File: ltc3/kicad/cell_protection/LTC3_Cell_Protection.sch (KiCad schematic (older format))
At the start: 80 parts, among them P301 CONN_BATT_MAIN, P303 CONN_BATT_SENSE, P305 S2BPHKS, P306 PIN_HEAD_1x2, Q301 MMBT3904, Q302 SUM110P08-11, Q303 SUM110P08-11, Q304 SUM110P08-11, Q305 SUM110P08-11, Q306 NDS9407, U301 LTC2990, U302 BQ77PL900

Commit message: LTC3: Charge Controller Layout
With boards broken up, charge controller circuitry has been re-layed out.
This commit is a rough first pass - there is no via stiching to ground
yet.
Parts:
- renumbered BT301 to BT1, BT302 to BT2, BT303 to BT3, BT304 to BT4, BT305 to BT5, BT306 to BT6, BT307 to BT7, BT308 to BT8, C313 to C1, C304 to C10, C310 to C11, C311 to C12, C312 to C13, C315 to C14, C317 to C15, C318 to C16, C319 to C17, C306 to C18, C302 to C19, C305 to C2, C301 to C20, C314 to C3, C316 to C4, C307 to C5, C303 to C6, C308 to C7, C309 to C8, C320 to C9, D301 to D1, D302 to D2, D305 to D3, D303 to D4, D306 to D5, D304 to D6, F301 to F1, P305 to P1, P306 to P2, P301 to P3, P303 to P4, P302 to P5, P304 to P6, Q302 to Q1, Q304 to Q2, Q306 to Q3, Q303 to Q4, Q305 to Q5, Q301 to Q6, R303 to R1, R324 to R10, R323 to R11, R305 to R12, R310 to R13, R312 to R14, R313 to R15, R314 to R16, R316 to R17, R317 to R18, R319 to R19, R307 to R2, R320 to R20, R321 to R21, R306 to R22, R302 to R23, R301 to R24, R308 to R3, R315 to R4, R318 to R5, R304 to R6, R309 to R7, R311 to R8, R322 to R9, U302 to U1, U301 to U2, W302 to W1, W306 to W2, W307 to W3, W304 to W4, W305 to W5, W301 to W6, W303 to W7

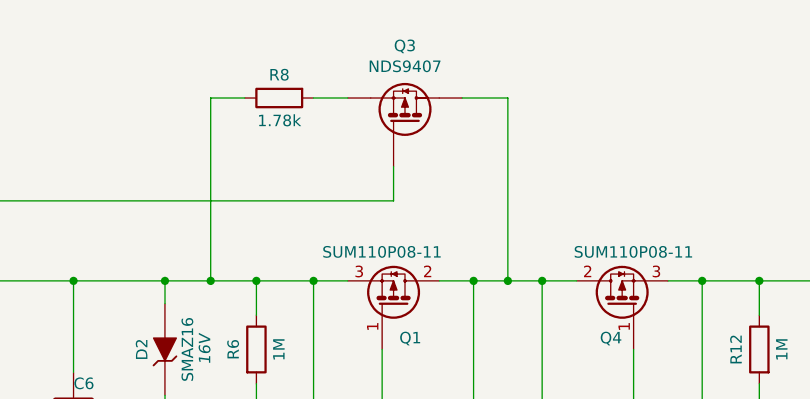
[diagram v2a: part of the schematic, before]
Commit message: LTC3: Restarted layout of Cell Protection
Began re-laying out cell protection section of LTC3.
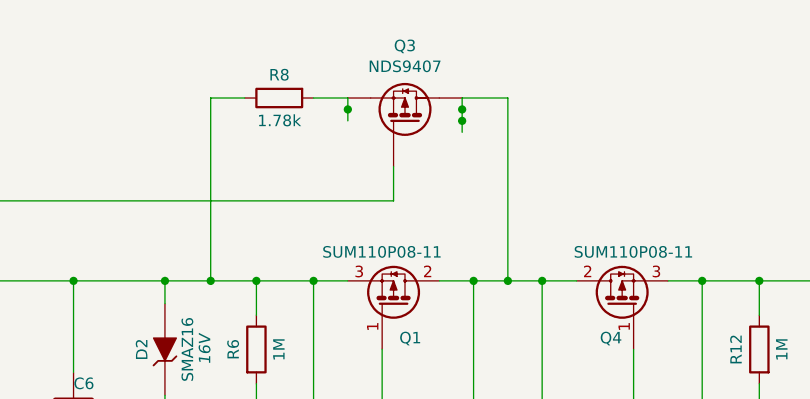
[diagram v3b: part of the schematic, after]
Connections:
- net at Q3.3 (S), R8.2: now also Q3.1 (S), Q3.2 (S)
- net at Q1.2, Q2.2, Q3.5 (D)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: now also Q3.6 (D), Q3.7 (D), Q3.8 (D)
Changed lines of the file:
@@
 Text Notes 9100 5650 0    100  ~ 20
 TODO: select connectors
+Wire Wire Line
+	4250 1100 4250 1250
+Connection ~ 4250 1150
+Connection ~ 4250 1200
+Wire Wire Line
+	3750 1100 3750 1200
+Connection ~ 3750 1150
 $EndSCHEMATC

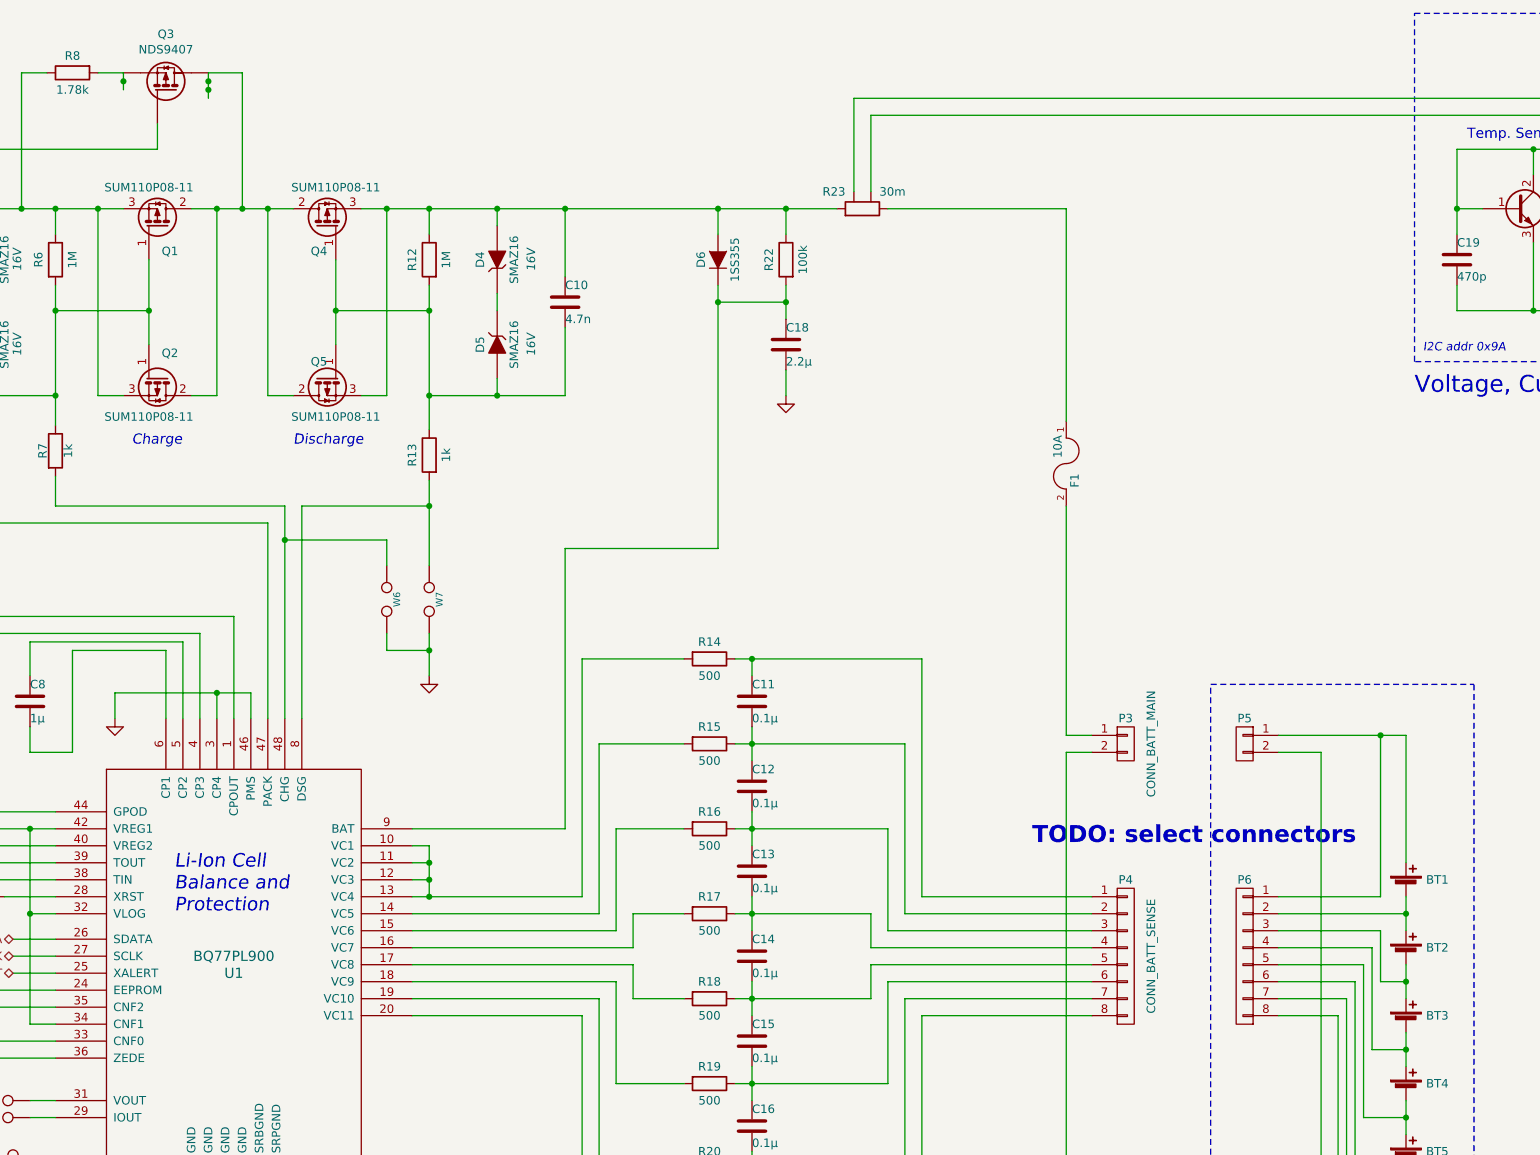
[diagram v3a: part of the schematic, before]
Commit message: LTC3: Selected battery connectors for cell protection board.
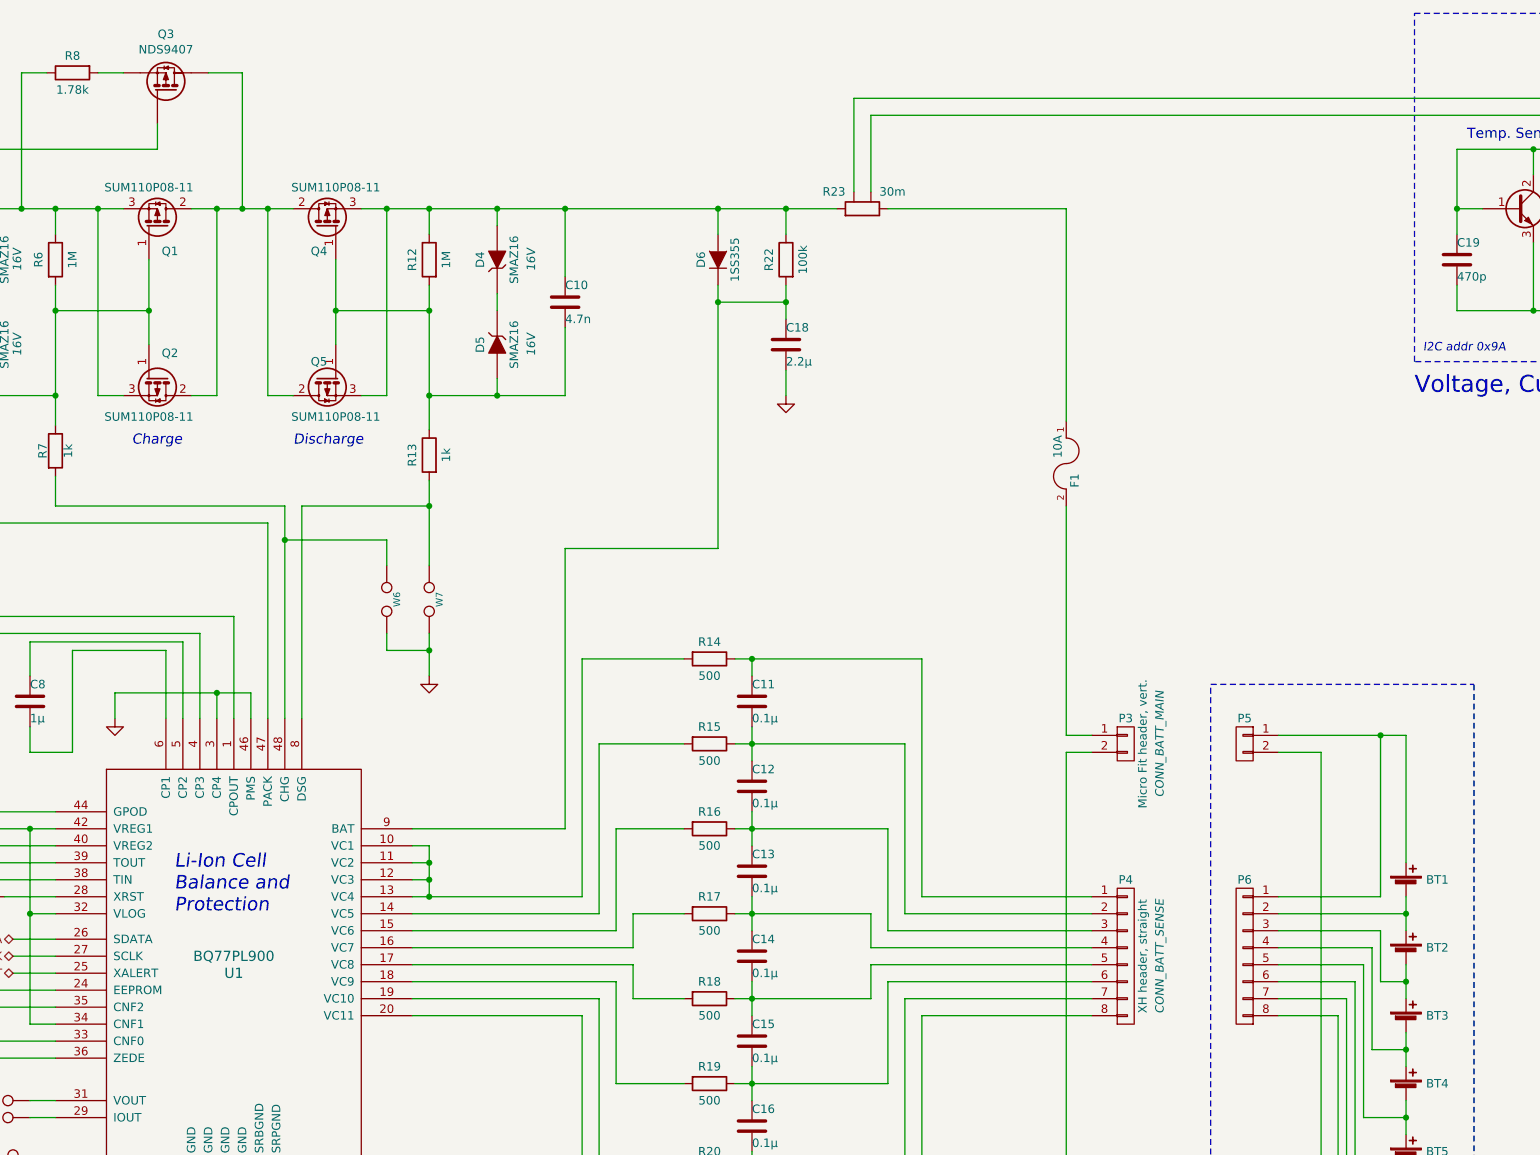
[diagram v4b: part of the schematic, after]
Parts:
- F1: Mfg_Name (none) -> Keystone; Mfg_PN (none) -> 3557-2; Note (none) -> -; Spec (none) -> -
- P3: value CONN_BATT_MAIN -> Micro Fit header, vert.; Mfg_Name (none) -> Molex; Mfg_PN (none) -> 43045-0228; Note (none) -> CONN_BATT_MAIN; Spec (none) -> -
- P4: value CONN_BATT_SENSE -> XH header, straight; footprint Connectors_Molex:Molex_Microfit3_Header_02x04_Straight_43045-0828 -> Connectors_JST:JST_XH_B08B-XH-A_08x2.50mm_Straight; Mfg_Name (none) -> JST; Mfg_PN (none) -> B8B-XH-A; Note (none) -> CONN_BATT_SENSE; Spec (none) -> -
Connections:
- net at Q3.3 (S), R8.2: no longer Q3.1 (S), Q3.2 (S)
- net at Q1.2, Q2.2, Q3.5 (D)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: no longer Q3.6 (D), Q3.7 (D), Q3.8 (D)
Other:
- note removed: "TODO: select connectors"
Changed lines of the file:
@@
 LIBS:atmel
 LIBS:audio
-LIBS:bbd
 LIBS:brooktre
 LIBS:cmos4000
@@
 P 9650 6300
 F 0 "P4" H 9650 6750 50  0000 C CNN
-F 1 "CONN_BATT_SENSE" V 9800 6300 50  0000 C CNN
-F 2 "Connectors_Molex:Molex_Microfit3_Header_02x04_Straight_43045-0828" H 9650 6300 60  0001 C CNN
-F 3 "" H 9650 6300 60  0000 C CNN
+F 1 "XH header, straight" V 9750 6300 50  0000 C CNN
+F 2 "Connectors_JST:JST_XH_B08B-XH-A_08x2.50mm_Straight" H 9650 6300 60  0001 C CNN
+F 3 "http://www.jst-mfg.com/product/pdf/eng/eXH.pdf" H 9650 6300 60  0001 C CNN
+F 4 "-" H 9650 6300 60  0001 C CNN "Spec"
+F 5 "CONN_BATT_SENSE" V 9850 6300 50  0000 C CIN "Note"
+F 6 "JST" H 9650 6300 60  0001 C CNN "Mfg_Name"
+F 7 "B8B-XH-A" H 9650 6300 60  0001 C CNN "Mfg_PN"
 	1    9650 6300
 	1    0    0    -1
@@
 P 9650 5050
 F 0 "P3" H 9650 5200 50  0000 C CNN
-F 1 "CONN_BATT_MAIN" V 9800 5050 50  0000 C CNN
+F 1 "Micro Fit header, vert." V 9750 5050 50  0000 C CNN
 F 2 "Connectors_Molex:Molex_Microfit3_Header_02x01_Straight_43045-0228" H 9650 5050 60  0001 C CNN
 F 3 "" H 9650 5050 60  0000 C CNN
+F 4 "-" H 9650 5050 60  0001 C CNN "Spec"
+F 5 "CONN_BATT_MAIN" V 9850 5050 50  0000 C CIN "Note"
+F 6 "Molex" H 9650 5050 60  0001 C CNN "Mfg_Name"
+F 7 "43045-0228" H 9650 5050 60  0001 C CNN "Mfg_PN"
 	1    9650 5050
 	1    0    0    -1
@@
 F 2 "LTC3:Fuseholder_Auto_Blade_Regular_Keystone_3557-2" H 9300 3400 60  0001 C CNN
 F 3 "" H 9300 3400 60  0000 C CNN
+F 4 "-" H 9300 3400 60  0001 C CNN "Spec"
+F 5 "-" H 9300 3400 60  0001 C CNN "Note"
+F 6 "Keystone" H 9300 3400 60  0001 C CNN "Mfg_Name"
+F 7 "3557-2" H 9300 3400 60  0001 C CNN "Mfg_PN"
 	1    9300 3400
 	0    1    1    0
@@
 Wire Wire Line
 	2100 3100 2100 3000
-Text Notes 9100 5650 0    100  ~ 20
-TODO: select connectors
-Wire Wire Line
-	4250 1100 4250 1250
-Connection ~ 4250 1150
-Connection ~ 4250 1200
-Wire Wire Line
-	3750 1100 3750 1200
-Connection ~ 3750 1150
 $EndSCHEMATC

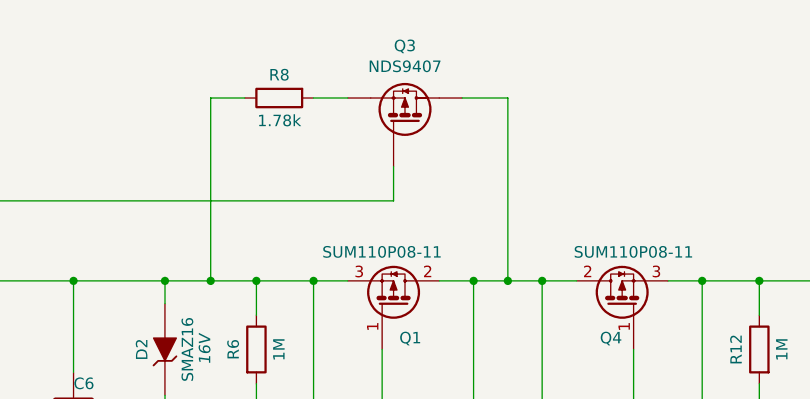
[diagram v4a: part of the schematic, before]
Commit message: LTC3: Cell Protection Layout
Made significant progress of Cell Protection board layout,
connected most nodes and began creating ground planes.

Reorganized mounting holes on Charge Controller
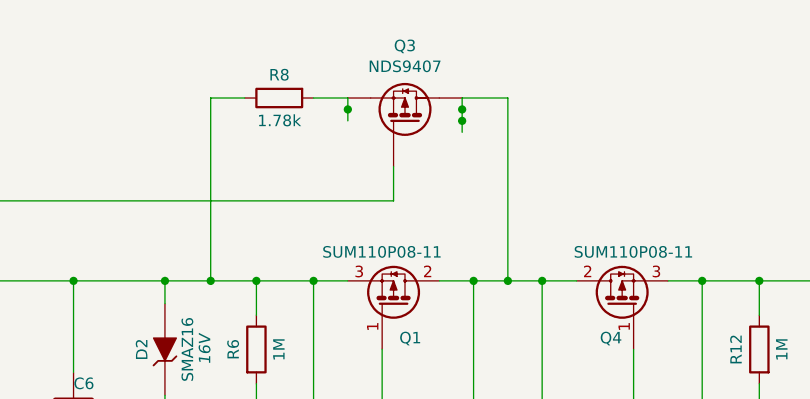
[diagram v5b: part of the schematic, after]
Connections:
- net at Q3.3 (S), R8.2: now also Q3.1 (S), Q3.2 (S)
- net at Q1.2, Q2.2, Q3.5 (D)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: now also Q3.6 (D), Q3.7 (D), Q3.8 (D)
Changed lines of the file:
@@
 LIBS:atmel
 LIBS:audio
+LIBS:bbd
 LIBS:brooktre
 LIBS:cmos4000
@@
 $EndComp
 $Comp
-L GND #PWR11
+L GND #PWR01
 U 1 1 564DE030
 P 4150 8000
-F 0 "#PWR11" H 4150 7750 50  0001 C CNN
+F 0 "#PWR01" H 4150 7750 50  0001 C CNN
 F 1 "GND" H 4150 7850 50  0001 C CNN
 F 2 "" H 4150 8000 60  0000 C CNN
@@
 $EndComp
 $Comp
-L GND #PWR6
+L GND #PWR02
 U 1 1 5650209A
 P 2300 5200
-F 0 "#PWR6" H 2300 4950 50  0001 C CNN
+F 0 "#PWR02" H 2300 4950 50  0001 C CNN
 F 1 "GND" H 2300 5050 50  0001 C CNN
 F 2 "" H 2300 5200 60  0000 C CNN
@@
 $EndComp
 $Comp
-L GND #PWR1
+L GND #PWR03
 U 1 1 5650665C
 P 700 6400
-F 0 "#PWR1" H 700 6150 50  0001 C CNN
+F 0 "#PWR03" H 700 6150 50  0001 C CNN
 F 1 "GND" H 700 6250 50  0001 C CNN
 F 2 "" H 700 6400 60  0000 C CNN
@@
 $EndComp
 $Comp
-L GND #PWR3
+L GND #PWR04
 U 1 1 5652F47D
 P 1050 3000
-F 0 "#PWR3" H 1050 2750 50  0001 C CNN
+F 0 "#PWR04" H 1050 2750 50  0001 C CNN
 F 1 "GND" H 1050 2850 50  0001 C CNN
 F 2 "" H 1050 3000 60  0000 C CNN
@@
 $EndComp
 $Comp
-L VBATT #PWR2
+L VBATT #PWR05
 U 1 1 5658A738
 P 1050 1650
-F 0 "#PWR2" H 1050 1500 50  0001 C CNN
+F 0 "#PWR05" H 1050 1500 50  0001 C CNN
 F 1 "VBATT" H 1050 1800 50  0000 C CNN
 F 2 "" H 1050 1650 60  0000 C CNN
@@
 $EndComp
 $Comp
-L +5V #PWR15
+L +5V #PWR06
 U 1 1 5659CAB5
 P 14300 1000
-F 0 "#PWR15" H 14300 850 50  0001 C CNN
+F 0 "#PWR06" H 14300 850 50  0001 C CNN
 F 1 "+5V" H 14300 1140 50  0000 C CNN
 F 2 "" H 14300 1000 60  0000 C CNN
@@
 $EndComp
 $Comp
-L GND #PWR16
+L GND #PWR07
 U 1 1 5659CACB
 P 14300 2550
-F 0 "#PWR16" H 14300 2300 50  0001 C CNN
+F 0 "#PWR07" H 14300 2300 50  0001 C CNN
 F 1 "GND" H 14300 2400 50  0001 C CNN
 F 2 "" H 14300 2550 60  0000 C CNN
@@
 $EndComp
 $Comp
-L GND #PWR17
+L GND #PWR08
 U 1 1 565C67AD
 P 15200 2450
-F 0 "#PWR17" H 15200 2200 50  0001 C CNN
+F 0 "#PWR08" H 15200 2200 50  0001 C CNN
 F 1 "GND" H 15200 2300 50  0001 C CNN
 F 2 "" H 15200 2450 60  0000 C CNN
@@
 $EndComp
 $Comp
-L GND #PWR14
+L GND #PWR09
 U 1 1 565B72B8
 P 7650 3000
-F 0 "#PWR14" H 7650 2750 50  0001 C CNN
+F 0 "#PWR09" H 7650 2750 50  0001 C CNN
 F 1 "GND" H 7650 2850 50  0001 C CNN
 F 2 "" H 7650 3000 60  0000 C CNN
@@
 $EndComp
 $Comp
-L GND #PWR10
+L GND #PWR010
 U 1 1 565D2BB8
 P 3700 4900
-F 0 "#PWR10" H 3700 4650 50  0001 C CNN
+F 0 "#PWR010" H 3700 4650 50  0001 C CNN
 F 1 "GND" H 3700 4750 50  0001 C CNN
 F 2 "" H 3700 4900 60  0000 C CNN
@@
 $EndComp
 $Comp
-L GND #PWR8
+L GND #PWR011
 U 1 1 565F5A93
 P 2675 7050
-F 0 "#PWR8" H 2675 6800 50  0001 C CNN
+F 0 "#PWR011" H 2675 6800 50  0001 C CNN
 F 1 "GND" H 2675 6900 50  0001 C CNN
 F 2 "" H 2675 7050 60  0000 C CNN
@@
 $EndComp
 $Comp
-L GND #PWR4
+L GND #PWR012
 U 1 1 565FA5A2
 P 1300 7100
-F 0 "#PWR4" H 1300 6850 50  0001 C CNN
+F 0 "#PWR012" H 1300 6850 50  0001 C CNN
 F 1 "GND" H 1300 6950 50  0001 C CNN
 F 2 "" H 1300 7100 60  0000 C CNN
@@
 $EndComp
 $Comp
-L GND #PWR12
+L GND #PWR013
 U 1 1 565E5619
 P 4550 9200
-F 0 "#PWR12" H 4550 8950 50  0001 C CNN
+F 0 "#PWR013" H 4550 8950 50  0001 C CNN
 F 1 "GND" H 4550 9050 50  0001 C CNN
 F 2 "" H 4550 9200 60  0000 C CNN
@@
 $EndComp
 $Comp
-L GND #PWR13
+L GND #PWR014
 U 1 1 56CBF3B2
 P 5550 4650
-F 0 "#PWR13" H 5550 4400 50  0001 C CNN
+F 0 "#PWR014" H 5550 4400 50  0001 C CNN
 F 1 "GND" H 5550 4500 50  0001 C CNN
 F 2 "" H 5550 4650 60  0000 C CNN
@@
 $EndComp
 $Comp
-L GND #PWR7
+L GND #PWR015
 U 1 1 56E4B689
 P 2500 7750
-F 0 "#PWR7" H 2500 7500 50  0001 C CNN
+F 0 "#PWR015" H 2500 7500 50  0001 C CNN
 F 1 "GND" H 2500 7600 50  0001 C CNN
 F 2 "" H 2500 7750 60  0000 C CNN
@@
 $EndComp
 $Comp
-L GND #PWR9
+L GND #PWR016
 U 1 1 56E4A519
 P 3100 7750
-F 0 "#PWR9" H 3100 7500 50  0001 C CNN
+F 0 "#PWR016" H 3100 7500 50  0001 C CNN
 F 1 "GND" H 3108 7577 50  0001 C CNN
 F 2 "" H 3100 7750 50  0000 C CNN
@@
 Connection ~ 2100 2450
 $Comp
-L GND #PWR5
+L GND #PWR017
 U 1 1 573455B4
 P 2100 3100
-F 0 "#PWR5" H 2100 2850 50  0001 C CNN
+F 0 "#PWR017" H 2100 2850 50  0001 C CNN
 F 1 "GND" H 2105 2927 50  0000 C CNN
 F 2 "" H 2100 3100 50  0000 C CNN
@@
 Wire Wire Line
 	2100 3100 2100 3000
+Wire Wire Line
+	4250 1100 4250 1250
+Connection ~ 4250 1150
+Connection ~ 4250 1200
+Wire Wire Line
+	3750 1100 3750 1200
+Connection ~ 3750 1150
 $EndSCHEMATC

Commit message: LTC3: Added Vbatt connectors to cell protection board.
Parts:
- added P7, P8: MicroFit head., Connectors_Molex:Molex_Microfit3_Header_02x01_Straight_43045-0228, symbol CONN_01X02
- P3: value Micro Fit header, vert. -> MicroFit header
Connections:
- net GND: now also P7.2 (P2), P8.2 (P2)
- net VBATT: now also P7.1 (P1), P8.1 (P1)
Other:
- moved on the sheet: BT1, BT2, BT3, BT4, BT5, BT6, BT7, BT8, C1, C10, C11, C12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
